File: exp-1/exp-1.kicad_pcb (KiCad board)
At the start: 4 copper layers, 50.8 x 50.8 mm, 90 parts, among them Q1 2n5109, U1 ABA-52563, U2 AVT-50663, U3 ABA-52563, U4 AVT-50663, U5 ADE-1

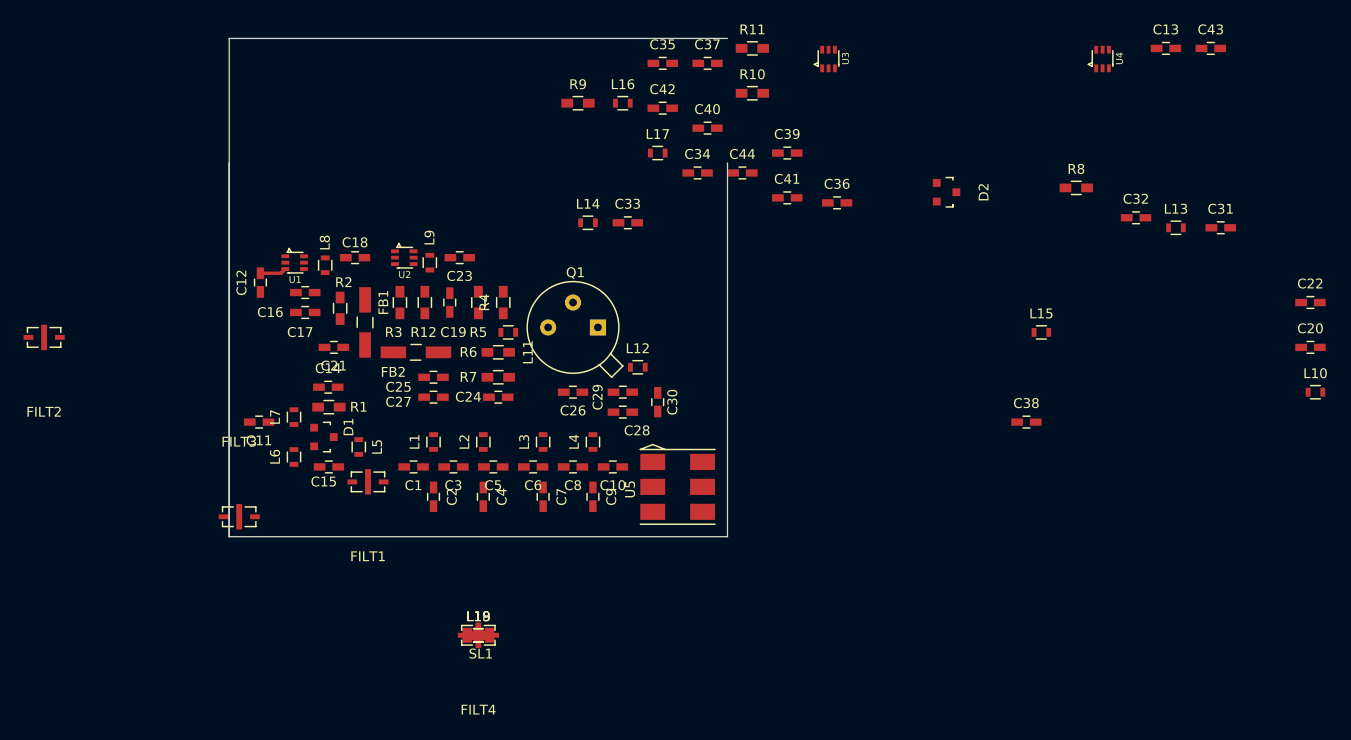
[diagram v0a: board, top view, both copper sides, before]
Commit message: Finished first round of routing. Power circuitry and breakout still needed.
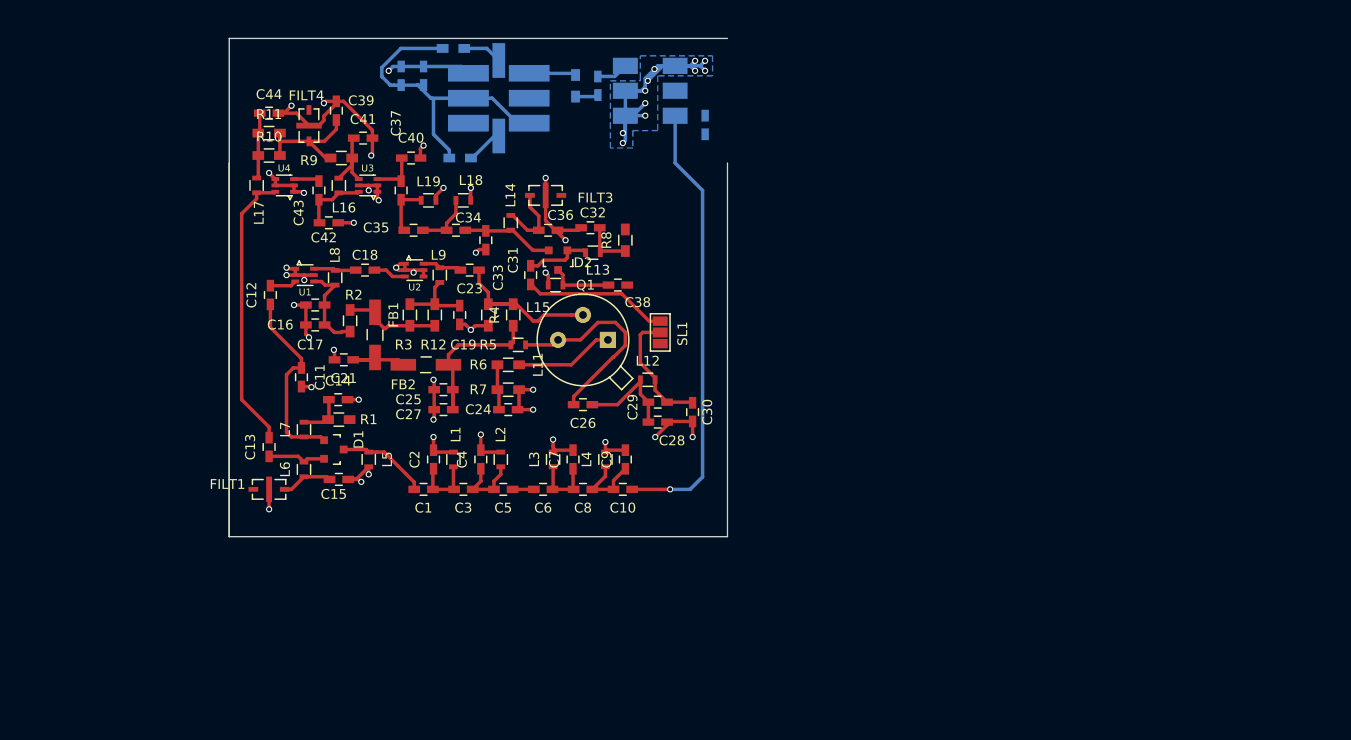
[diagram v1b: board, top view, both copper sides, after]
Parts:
- removed FILT2: MTFILT, exp-1:FILTACH32T
- removed L10: .33u, Resistors_SMD:R_0603
- added C45: 470p, Capacitors_SMD:C_0603_HandSoldering, B.Cu at (111.8, 108.5)
- added C46: 470p, Capacitors_SMD:C_0603_HandSoldering, B.Cu at (122.7, 112.5)
- added R13: 1K, Resistors_SMD:R_0603_HandSoldering, B.Cu at (97.0, 104.6)
- added R14: 1K, Resistors_SMD:R_0603_HandSoldering, B.Cu at (97.7, 115.8)
- added R15: 38R, Resistors_SMD:R_0603_HandSoldering, B.Cu at (109.5, 108.5)
- added U6: Si570, exp-1:SI570-HS, B.Cu at (99.6, 112.3)
- C20: value 470p -> .01u; moved to B.Cu
- C22, U5: moved to B.Cu
- moved C13 100.1 mm to (78.2, 145.3), turned to 90 degrees
- moved C20 96.8 mm to (91.7, 107.4), turned to 90 degrees
- moved C22 93.3 mm to (94.0, 107.4), turned to 90 degrees
- moved C43 92.1 mm to (83.3, 119.1), turned to 270 degrees
- moved U4 82.8 mm to (80.8, 119.3), turned to 90 degrees
- moved C31 70.5 mm to (104.9, 127.8), turned to 90 degrees
- moved L13 59.5 mm to (111.3, 125.5)
- moved C32 55.6 mm to (111.0, 122.9), turned to 180 degrees
- moved FILT4 54.8 mm to (82.3, 112.5), turned to 90 degrees
- moved R11 50.0 mm to (78.2, 113.3)
- moved L15 49.8 mm to (107.4, 128.8), turned to 180 degrees
- moved R10 49.7 mm to (78.2, 115.6)
- moved C44 48.6 mm to (78.2, 111.3)
- moved U3 47.1 mm to (89.3, 119.3), turned to 90 degrees
- moved R8 46.3 mm to (114.6, 124.2), turned to 90 degrees
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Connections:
- C20 pad 1: Net-(C20-Pad1) -> +3.3V
- C20 pad 2: Net-(C20-Pad2) -> GND
- C22 pad 1: Net-(C22-Pad1) -> +3.3V
- C22 pad 2: Net-(C22-Pad2) -> GND
- C41 pad 1: Net-(C39-Pad1) -> Net-(C41-Pad1)
- L16 pad 1: Net-(C39-Pad1) -> Net-(C41-Pad1)
- R9 pad 2: Net-(C39-Pad1) -> Net-(C41-Pad1)
- U3 pad 4: Net-(C39-Pad1) -> Net-(C41-Pad1)
- U5 pad 2: /IF -> Net-(C46-Pad2)
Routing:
- net GND: track 0.00 -> 284.3 mm, vias 0 -> 51
- net Net-(C10-Pad1): track 0.00 -> 45.7 mm, vias 0 -> 1
- net +3.3V: track 0.00 -> 32.3 mm
- net Net-(C13-Pad2): track 0.00 -> 28.7 mm
- net Net-(C26-Pad2): track 0.00 -> 21.3 mm
- net Net-(C11-Pad1): track 0.00 -> 19.6 mm
- net Net-(C23-Pad1): track 0.00 -> 17.0 mm
- net Net-(C25-Pad1): track 0.00 -> 16.6 mm
- net /TX_SL: track 0.00 -> 14.8 mm
- net Net-(C39-Pad1): track 0.00 -> 13.2 mm
- net /TX_P: track 0.00 -> 12.8 mm
- net Net-(C26-Pad1): track 0.00 -> 10.7 mm
- net Net-(Q1-Pad1): track 0.00 -> 10.1 mm
- net Net-(FB1-Pad1): track 0.00 -> 9.95 mm
- net Net-(C16-Pad1): track 0.00 -> 9.79 mm
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- added copper zone on B.Cu, net GND
- added copper zone on In1.Cu, net GND
- added copper zone on In2.Cu, net GND
